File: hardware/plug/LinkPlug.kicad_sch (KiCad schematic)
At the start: 6 parts, among them J301 SJ2-25404B-SMT-TR, U301 TLP2361

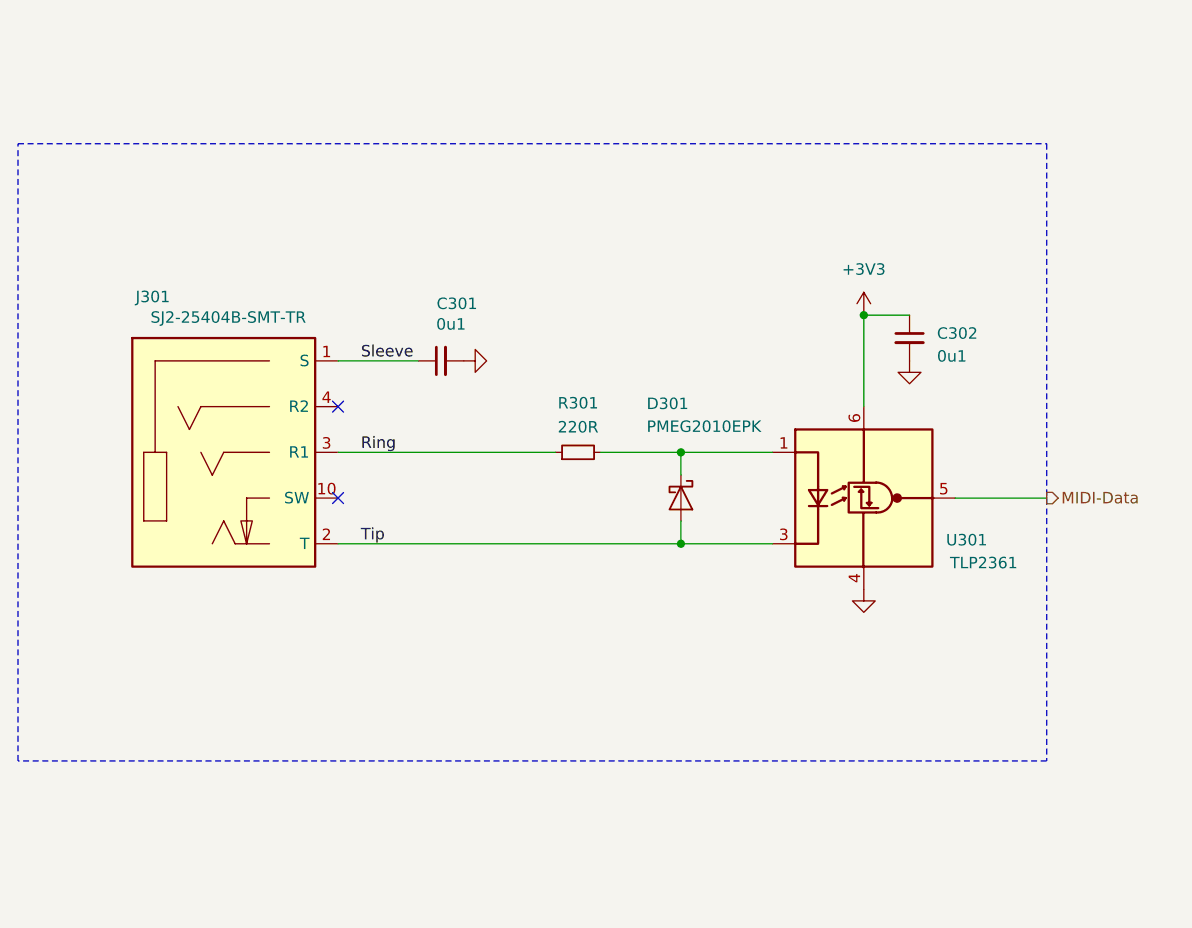
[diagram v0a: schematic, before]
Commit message: Split into socket and plug
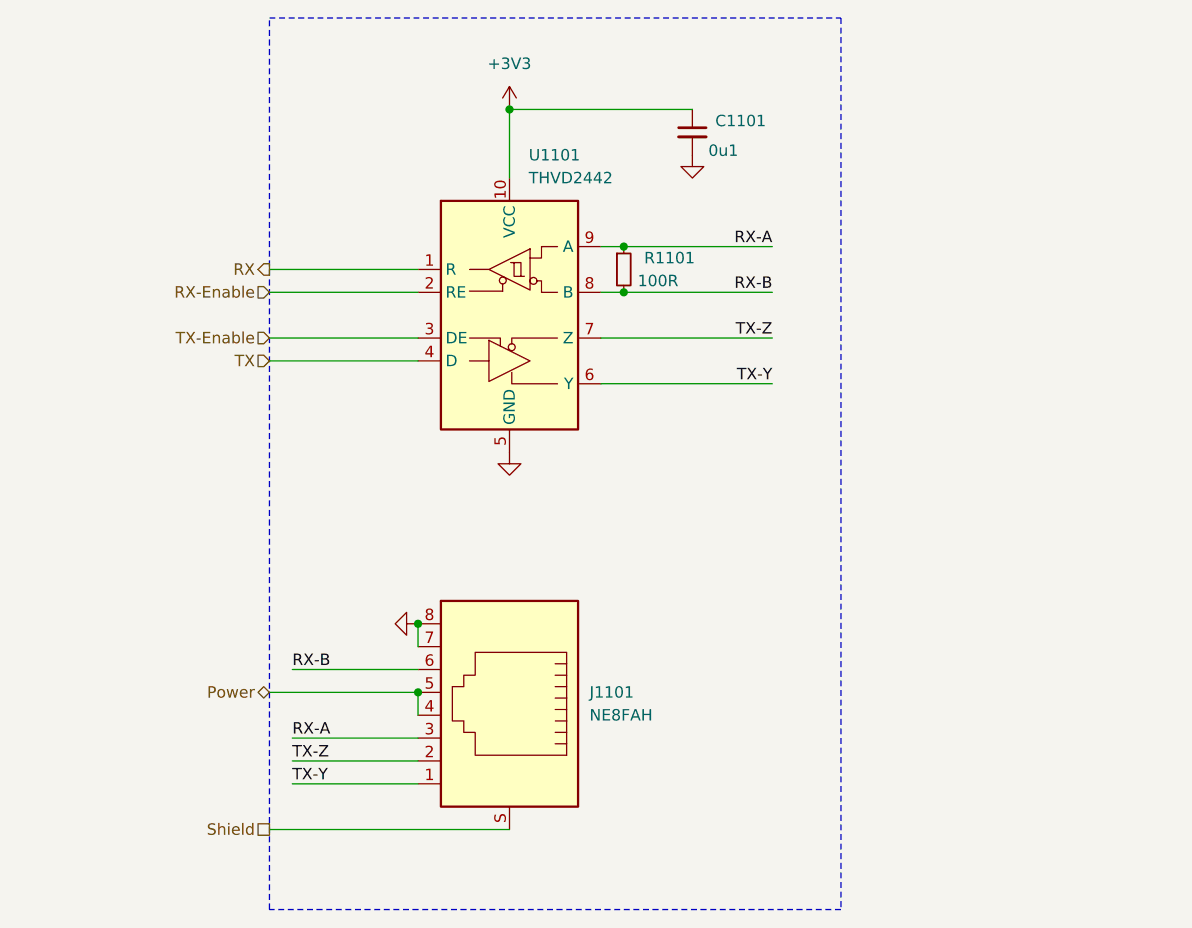
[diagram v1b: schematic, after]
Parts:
- removed C301, C302: 0u1, V2_Capacitor_SMD:C_0603, symbol V2_Capacitor:0603_0u1
- removed D301: PMEG2010EPK, V2_Diode_SMD:D_SOD-1608, symbol V2_Diode:PMEG2010EPK
- removed J301: SJ2-25404B-SMT-TR, V2_Connector_Audio:CUI_SJ2-25404B-SMT-TR, symbol V2_Connector_Audio:SJ2-25404B-SMT-TR
- removed R301: 220R, V2_Resistor_SMD:R_0603, symbol V2_Resistor:0603_220R
- removed U301: TLP2361, V2_Package_SO:SO-5-6_4.55x3.7mm_P1.27mm, symbol V2_Isolator:TLP2361
- added C1101: 0u1, V2_Capacitor_SMD:C_0603, symbol V2_Capacitor:0603_0u1
- added J1101: NE8FAH, V2_Connector_EtherCon:NE8FAH, symbol V2_Connector_EtherCon:NE8FAH
- added R1101: 100R, V2_Resistor_SMD:R_0603, symbol V2_Resistor:0603_100R
- added U1101: THVD2442, V2_Package_SON:VSON-10-4-1EP_3x3mm_P0.5mm_EP1.65x2.4mm_ThermalVias, symbol V2_Interface_RS485:THVD2442
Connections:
- net +3V3: now also C1101.1, U1101.10 (VCC)
- net GND: now also C1101.2, J1101.7, J1101.8, U1101.11 (GND), U1101.5 (GND)
- new net Power: J1101.4, J1101.5
- new net RX: U1101.1 (R)
- new net RX-A: J1101.3, R1101.1, U1101.9 (A)
- new net RX-B: J1101.6, R1101.2, U1101.8 (B)
- new net RX-Enable: U1101.2 (RE)
- new net Shield: J1101.S
- new net TX: U1101.4 (D)
- new net TX-Enable: U1101.3 (DE)
- new net TX-Y: J1101.1, U1101.6 (Y)
- new net TX-Z: J1101.2, U1101.7 (Z)
- no-connect marks 2 -> 0
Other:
- title: V2 connect -> V2 connect-plug

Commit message: Good Bye Imperial
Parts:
- C1101: footprint V2_Capacitor_SMD:C_0603 -> V2_Capacitor_SMD:C_1608; symbol V2_Capacitor:0603_0u1 -> V2_Capacitor:1608_0u1
- R1101: footprint V2_Resistor_SMD:R_0603 -> V2_Resistor_SMD:R_1608; symbol V2_Resistor:0603_100R -> V2_Resistor:1608_100R
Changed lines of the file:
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@@
+			)
+		)
+		(property "LCSC" ""
+			(at 148.59 92.71 0)
+			(hide yes)
+			(show_name no)
+			(do_not_autoplace no)
+			(effects
+				(font
+					(size 1.27 1.27)
+				)
+			)
+		)
+		(property "Sim.Enable" ""
+			(at 148.59 92.71 0)
+			(hide yes)
+			(show_name no)
+			(do_not_autoplace no)
+			(effects
+				(font
+					(size 1.27 1.27)
+				)
+			)
+		)
+		(property "Voltage" ""
+			(at 148.59 92.71 0)
+			(hide yes)
+			(show_name no)
+			(do_not_autoplace no)
+			(effects
+				(font
+					(size 1.27 1.27)
+				)
 			)
 		)
@@
 	)
 	(symbol
-		(lib_id "V2_Resistor:0603_100R")
+		(lib_id "V2_Resistor:1608_100R")
 		(at 161.29 87.63 0)
 		(unit 1)
@@
 			)
 		)
-		(property "Footprint" "V2_Resistor_SMD:R_0603"
+		(property "Footprint" "V2_Resistor_SMD:R_1608"
 			(at 161.29 103.378 0)
 			(hide yes)
@@
 		(property "Id" "Resistor:${SYMBOL_NAME}"
 			(at 161.29 101.6 0)
+			(hide yes)
+			(show_name no)
+			(do_not_autoplace no)
+			(effects
+				(font
+					(size 1.27 1.27)
+				)
+			)
+		)
+		(property "LCSC" ""
+			(at 161.29 87.63 0)
+			(hide yes)
+			(show_name no)
+			(do_not_autoplace no)
+			(effects
+				(font
+					(size 1.27 1.27)
+				)
+			)
+		)
+		(property "Sim.Enable" ""
+			(at 161.29 87.63 0)
+			(hide yes)
+			(show_name no)
+			(do_not_autoplace no)
+			(effects
+				(font
+					(size 1.27 1.27)
+				)
+			)
+		)
+		(property "Voltage" ""
+			(at 161.29 87.63 0)
 			(hide yes)
 			(show_name no)
@@
 			)
 		)
+		(property "LCSC" ""
+			(at 148.59 137.16 0)
+			(hide yes)
+			(show_name no)
+			(do_not_autoplace no)
+			(effects
+				(font
+					(size 1.27 1.27)
+				)
+			)
+		)
+		(property "Sim.Enable" ""
+			(at 148.59 137.16 0)
+			(hide yes)
+			(show_name no)
+			(do_not_autoplace no)
+			(effects
+				(font
+					(size 1.27 1.27)
+				)
+			)
+		)
+		(property "Voltage" ""
+			(at 148.59 137.16 0)
+			(hide yes)
+			(show_name no)
+			(do_not_autoplace no)
+			(effects
+				(font
+					(size 1.27 1.27)
+				)
+			)
+		)
 		(pin "7"
 		)
@@
 	)
 	(symbol
-		(lib_id "V2_Capacitor:0603_0u1")
+		(lib_id "V2_Capacitor:1608_0u1")
 		(at 168.91 72.39 0)
 		(unit 1)
@@
 			)
 		)
-		(property "Footprint" "V2_Capacitor_SMD:C_0603"
+		(property "Footprint" "V2_Capacitor_SMD:C_1608"
 			(at 168.91 89.408 0)
 			(hide yes)
@@
 			(hide yes)
 			(show_name no)
+			(do_not_autoplace no)
+			(effects
+				(font
+					(size 1.27 1.27)
+				)
+			)
+		)
+		(property "LCSC" ""
+			(at 168.91 72.39 0)
+			(hide yes)
+			(show_name no)
+			(do_not_autoplace no)
+			(effects
+				(font
+					(size 1.27 1.27)
+				)
+			)
+		)
+		(property "Sim.Enable" ""
+			(at 168.91 72.39 0)
+			(hide yes)
+			(show_name no)
+			(do_not_autoplace no)
+			(effects
+				(font
+					(size 1.27 1.27)
+				)
+			)
+		)
+		(property "Voltage" ""
+			(at 168.91 72.39 0)
+			(hide yes)
+			(show_name no)

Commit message: Refresh
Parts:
- renumbered C1101 to C301, J1101 to J301, R1101 to R301, U1101 to U301
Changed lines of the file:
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@@
 		(in_pos_files yes)
 		(dnp no)
-		(property "Reference" "#PWR01104"
+		(property "Reference" "#PWR0304"
 			(at 168.91 81.28 0)
 			(hide yes)
@@
 			(project "plug"
 				(path "/6c8448b4-b04d-47e1-934e-e40cbe27a7be/be5efeaa-f0dd-4882-b2f8-53c61e0a33bd"
-					(reference "#PWR01104")
+					(reference "#PWR0304")
 					(unit 1)
 				)
@@
 		(dnp no)
 		(fields_autoplaced yes)
-		(property "Reference" "U1101"
+		(property "Reference" "U301"
 			(at 150.7333 74.93 0)
 			(show_name no)
@@
 		)
 		(property "LCSC" ""
-			(at 148.59 92.71 0)
-			(hide yes)
-			(show_name no)
-			(do_not_autoplace no)
-			(effects
-				(font
-					(size 1.27 1.27)
-				)
-			)
-		)
-		(property "Sim.Enable" ""
 			(at 148.59 92.71 0)
 			(hide yes)
@@
 			(project "plug"
 				(path "/6c8448b4-b04d-47e1-934e-e40cbe27a7be/be5efeaa-f0dd-4882-b2f8-53c61e0a33bd"
-					(reference "U1101")
+					(reference "U301")
 					(unit 1)
 				)
@@
 		(in_pos_files yes)
 		(dnp no)
-		(property "Reference" "R1101"
-			(at 166.37 86.36 0)
+		(property "Reference" "R301"
+			(at 165.862 86.614 0)
 			(show_name no)
 			(do_not_autoplace no)
@@
 		)
 		(property "Value" "100R"
-			(at 165.1 88.9 0)
+			(at 165.862 88.9 0)
 			(show_name no)
 			(do_not_autoplace no)
@@
 		)
 		(property "LCSC" ""
-			(at 161.29 87.63 0)
-			(hide yes)
-			(show_name no)
-			(do_not_autoplace no)
-			(effects
-				(font
-					(size 1.27 1.27)
-				)
-			)
-		)
-		(property "Sim.Enable" ""
 			(at 161.29 87.63 0)
 			(hide yes)
@@
 			(project "plug"
 				(path "/6c8448b4-b04d-47e1-934e-e40cbe27a7be/be5efeaa-f0dd-4882-b2f8-53c61e0a33bd"
-					(reference "R1101")
+					(reference "R301")
 					(unit 1)
 				)
@@
 		(dnp no)
 		(fields_autoplaced yes)
-		(property "Reference" "J1101"
+		(property "Reference" "J301"
 			(at 157.48 134.6199 0)
 			(show_name no)
@@
 		)
 		(property "LCSC" ""
-			(at 148.59 137.16 0)
-			(hide yes)
-			(show_name no)
-			(do_not_autoplace no)
-			(effects
-				(font
-					(size 1.27 1.27)
-				)
-			)
-		)
-		(property "Sim.Enable" ""
 			(at 148.59 137.16 0)
 			(hide yes)
@@
 			(project "plug"
 				(path "/6c8448b4-b04d-47e1-934e-e40cbe27a7be/be5efeaa-f0dd-4882-b2f8-53c61e0a33bd"
-					(reference "J1101")
+					(reference "J301")
 					(unit 1)
 				)
@@
 		(in_pos_files yes)
 		(dnp no)
-		(property "Reference" "#PWR01103"
+		(property "Reference" "#PWR0303"
 			(at 148.59 114.3 0)
 			(hide yes)
@@
 			(project "plug"
 				(path "/6c8448b4-b04d-47e1-934e-e40cbe27a7be/be5efeaa-f0dd-4882-b2f8-53c61e0a33bd"
-					(reference "#PWR01103")
+					(reference "#PWR0303")
 					(unit 1)
 				)
@@
 		(in_pos_files yes)
 		(dnp no)
-		(property "Reference" "#PWR01102"
+		(property "Reference" "#PWR0302"
 			(at 148.59 73.66 0)
 			(hide yes)
@@
 			(project "plug"
 				(path "/6c8448b4-b04d-47e1-934e-e40cbe27a7be/be5efeaa-f0dd-4882-b2f8-53c61e0a33bd"
-					(reference "#PWR01102")
+					(reference "#PWR0302")
 					(unit 1)
 				)
@@
 		(in_pos_files yes)
 		(dnp no)
-		(property "Reference" "C1101"
+		(property "Reference" "C301"
 			(at 171.45 71.1262 0)
 			(show_name no)
@@
 		)
 		(property "LCSC" ""
-			(at 168.91 72.39 0)
-			(hide yes)
-			(show_name no)
-			(do_not_autoplace no)
-			(effects
-				(font
-					(size 1.27 1.27)
-				)
-			)
-		)
-		(property "Sim.Enable" ""
 			(at 168.91 72.39 0)
 			(hide yes)
@@
 			(project "plug"
 				(path "/6c8448b4-b04d-47e1-934e-e40cbe27a7be/be5efeaa-f0dd-4882-b2f8-53c61e0a33bd"
-					(reference "C1101")
+					(reference "C301")
 					(unit 1)
 				)
@@
 		(in_pos_files yes)
 		(dnp no)
-		(property "Reference" "#PWR01101"
+		(property "Reference" "#PWR0301"
 			(at 132.08 127 0)
 			(hide yes)
@@
 			(project "plug"
 				(path "/6c8448b4-b04d-47e1-934e-e40cbe27a7be/be5efeaa-f0dd-4882-b2f8-53c61e0a33bd"
-					(reference "#PWR01101")
+					(reference "#PWR0301")
 					(unit 1)
 				)
